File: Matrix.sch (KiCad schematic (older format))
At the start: 171 parts

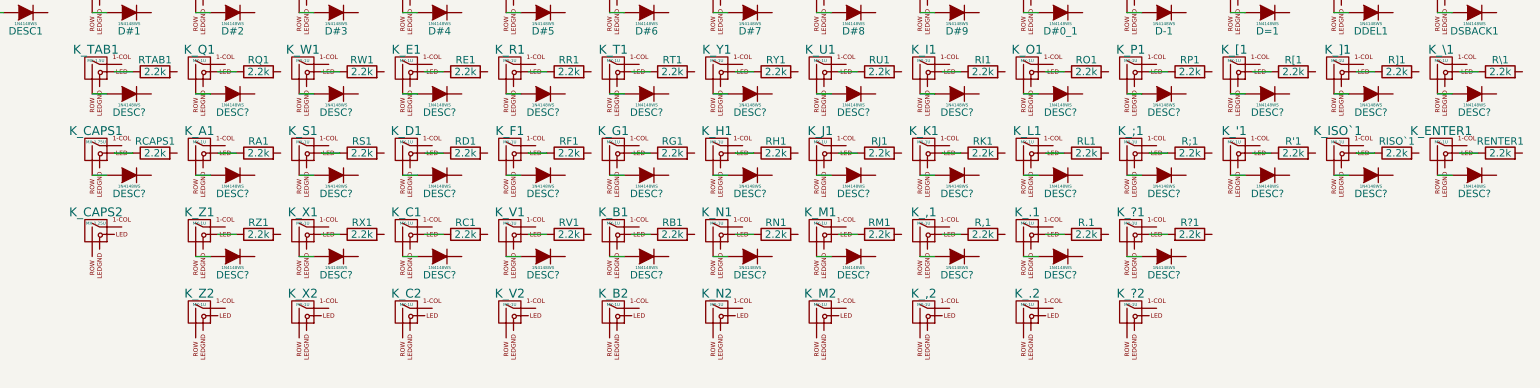
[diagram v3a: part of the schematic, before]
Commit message: Rename diodes
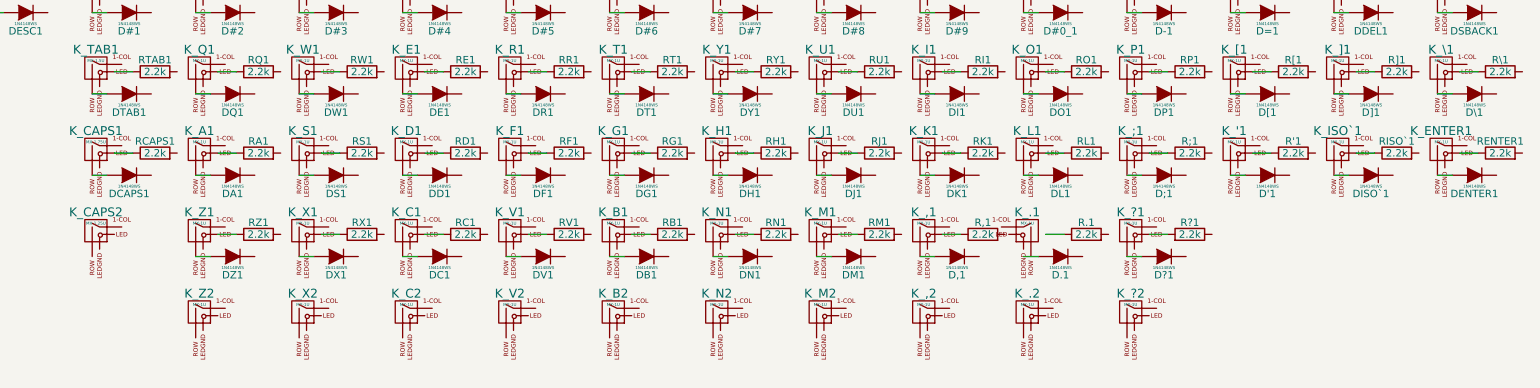
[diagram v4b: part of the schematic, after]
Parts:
- gave numbers to parts that had none: 38
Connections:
- net at K_.1.2 (ROW): no longer D.1.2 (A)
- net at K_.1.3 (LED): no longer R.1.1
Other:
- moved on the sheet: K_.1
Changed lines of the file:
@@
 $EndComp
 $Comp
-L D DESC?
+L D DTAB1
 U 1 1 597E3B71
 P 1725 2250
-F 0 "DESC?" H 1725 2375 50  0000 C CNN
+F 0 "DTAB1" H 1725 2375 50  0000 C CNN
 F 1 "1N4148WS" H 1725 2325 20  0000 C CNN
 F 2 "" H 1725 2250 50  0001 C CNN
@@
 $EndComp
 $Comp
-L D DESC?
+L D DQ1
 U 1 1 597E3B85
 P 2425 2250
-F 0 "DESC?" H 2425 2375 50  0000 C CNN
+F 0 "DQ1" H 2425 2375 50  0000 C CNN
 F 1 "1N4148WS" H 2425 2325 20  0000 C CNN
 F 2 "" H 2425 2250 50  0001 C CNN
@@
 $EndComp
 $Comp
-L D DESC?
+L D DW1
 U 1 1 597E3B99
 P 3125 2250
-F 0 "DESC?" H 3125 2375 50  0000 C CNN
+F 0 "DW1" H 3125 2375 50  0000 C CNN
 F 1 "1N4148WS" H 3125 2325 20  0000 C CNN
 F 2 "" H 3125 2250 50  0001 C CNN
@@
 $EndComp
 $Comp
-L D DESC?
+L D DE1
 U 1 1 597E3BAD
 P 3825 2250
-F 0 "DESC?" H 3825 2375 50  0000 C CNN
+F 0 "DE1" H 3825 2375 50  0000 C CNN
 F 1 "1N4148WS" H 3825 2325 20  0000 C CNN
 F 2 "" H 3825 2250 50  0001 C CNN
@@
 $EndComp
 $Comp
-L D DESC?
+L D DR1
 U 1 1 597E3BC1
 P 4525 2250
-F 0 "DESC?" H 4525 2375 50  0000 C CNN
+F 0 "DR1" H 4525 2375 50  0000 C CNN
 F 1 "1N4148WS" H 4525 2325 20  0000 C CNN
 F 2 "" H 4525 2250 50  0001 C CNN
@@
 $EndComp
 $Comp
-L D DESC?
+L D DT1
 U 1 1 597E3BD5
 P 5225 2250
-F 0 "DESC?" H 5225 2375 50  0000 C CNN
+F 0 "DT1" H 5225 2375 50  0000 C CNN
 F 1 "1N4148WS" H 5225 2325 20  0000 C CNN
 F 2 "" H 5225 2250 50  0001 C CNN
@@
 $EndComp
 $Comp
-L D DESC?
+L D DY1
 U 1 1 597E3BE9
 P 5925 2250
-F 0 "DESC?" H 5925 2375 50  0000 C CNN
+F 0 "DY1" H 5925 2375 50  0000 C CNN
 F 1 "1N4148WS" H 5925 2325 20  0000 C CNN
 F 2 "" H 5925 2250 50  0001 C CNN
@@
 $EndComp
 $Comp
-L D DESC?
+L D DU1
 U 1 1 597E3BFD
 P 6625 2250
-F 0 "DESC?" H 6625 2375 50  0000 C CNN
+F 0 "DU1" H 6625 2375 50  0000 C CNN
 F 1 "1N4148WS" H 6625 2325 20  0000 C CNN
 F 2 "" H 6625 2250 50  0001 C CNN
@@
 $EndComp
 $Comp
-L D DESC?
+L D DI1
 U 1 1 597E3C11
 P 7325 2250
-F 0 "DESC?" H 7325 2375 50  0000 C CNN
+F 0 "DI1" H 7325 2375 50  0000 C CNN
 F 1 "1N4148WS" H 7325 2325 20  0000 C CNN
 F 2 "" H 7325 2250 50  0001 C CNN
@@
 $EndComp
 $Comp
-L D DESC?
+L D DO1
 U 1 1 597E3C25
 P 8025 2250
-F 0 "DESC?" H 8025 2375 50  0000 C CNN
+F 0 "DO1" H 8025 2375 50  0000 C CNN
 F 1 "1N4148WS" H 8025 2325 20  0000 C CNN
 F 2 "" H 8025 2250 50  0001 C CNN
@@
 $EndComp
 $Comp
-L D DESC?
+L D DP1
 U 1 1 597E3C39
 P 8725 2250
-F 0 "DESC?" H 8725 2375 50  0000 C CNN
+F 0 "DP1" H 8725 2375 50  0000 C CNN
 F 1 "1N4148WS" H 8725 2325 20  0000 C CNN
 F 2 "" H 8725 2250 50  0001 C CNN
@@
 $EndComp
 $Comp
-L D DESC?
+L D D[1
 U 1 1 597E3C4D
 P 9425 2250
-F 0 "DESC?" H 9425 2375 50  0000 C CNN
+F 0 "D[1" H 9425 2375 50  0000 C CNN
 F 1 "1N4148WS" H 9425 2325 20  0000 C CNN
 F 2 "" H 9425 2250 50  0001 C CNN
@@
 $EndComp
 $Comp
-L D DESC?
+L D D]1
 U 1 1 597E3C61
 P 10125 2250
-F 0 "DESC?" H 10125 2375 50  0000 C CNN
+F 0 "D]1" H 10125 2375 50  0000 C CNN
 F 1 "1N4148WS" H 10125 2325 20  0000 C CNN
 F 2 "" H 10125 2250 50  0001 C CNN
@@
 $EndComp
 $Comp
-L D DESC?
+L D D\1
 U 1 1 597E3C75
 P 10825 2250
-F 0 "DESC?" H 10825 2375 50  0000 C CNN
+F 0 "D\\1" H 10825 2375 50  0000 C CNN
 F 1 "1N4148WS" H 10825 2325 20  0000 C CNN
 F 2 "" H 10825 2250 50  0001 C CNN
@@
 $EndComp
 $Comp
-L D DESC?
+L D DCAPS1
 U 1 1 597E5CB1
 P 1725 2800
-F 0 "DESC?" H 1725 2925 50  0000 C CNN
+F 0 "DCAPS1" H 1725 2925 50  0000 C CNN
 F 1 "1N4148WS" H 1725 2875 20  0000 C CNN
 F 2 "" H 1725 2800 50  0001 C CNN
@@
 $EndComp
 $Comp
-L D DESC?
+L D DA1
 U 1 1 597E5CC5
 P 2425 2800
-F 0 "DESC?" H 2425 2925 50  0000 C CNN
+F 0 "DA1" H 2425 2925 50  0000 C CNN
 F 1 "1N4148WS" H 2425 2875 20  0000 C CNN
 F 2 "" H 2425 2800 50  0001 C CNN
@@
 $EndComp
 $Comp
-L D DESC?
+L D DS1
 U 1 1 597E5CD9
 P 3125 2800
-F 0 "DESC?" H 3125 2925 50  0000 C CNN
+F 0 "DS1" H 3125 2925 50  0000 C CNN
 F 1 "1N4148WS" H 3125 2875 20  0000 C CNN
 F 2 "" H 3125 2800 50  0001 C CNN
@@
 $EndComp
 $Comp
-L D DESC?
+L D DD1
 U 1 1 597E5CED
 P 3825 2800
-F 0 "DESC?" H 3825 2925 50  0000 C CNN
+F 0 "DD1" H 3825 2925 50  0000 C CNN
 F 1 "1N4148WS" H 3825 2875 20  0000 C CNN
 F 2 "" H 3825 2800 50  0001 C CNN
@@
 $EndComp
 $Comp
-L D DESC?
+L D DF1
 U 1 1 597E5D01
 P 4525 2800
-F 0 "DESC?" H 4525 2925 50  0000 C CNN
+F 0 "DF1" H 4525 2925 50  0000 C CNN
 F 1 "1N4148WS" H 4525 2875 20  0000 C CNN
 F 2 "" H 4525 2800 50  0001 C CNN
@@
 $EndComp
 $Comp
-L D DESC?
+L D DG1
 U 1 1 597E5D15
 P 5225 2800
-F 0 "DESC?" H 5225 2925 50  0000 C CNN
+F 0 "DG1" H 5225 2925 50  0000 C CNN
 F 1 "1N4148WS" H 5225 2875 20  0000 C CNN
 F 2 "" H 5225 2800 50  0001 C CNN
@@
 $EndComp
 $Comp
-L D DESC?
+L D DH1
 U 1 1 597E5D29
 P 5925 2800
-F 0 "DESC?" H 5925 2925 50  0000 C CNN
+F 0 "DH1" H 5925 2925 50  0000 C CNN
 F 1 "1N4148WS" H 5925 2875 20  0000 C CNN
 F 2 "" H 5925 2800 50  0001 C CNN
@@
 $EndComp
 $Comp
-L D DESC?
+L D DJ1
 U 1 1 597E5D3D
 P 6625 2800
-F 0 "DESC?" H 6625 2925 50  0000 C CNN
+F 0 "DJ1" H 6625 2925 50  0000 C CNN
 F 1 "1N4148WS" H 6625 2875 20  0000 C CNN
 F 2 "" H 6625 2800 50  0001 C CNN
@@
 $EndComp
 $Comp
-L D DESC?
+L D DK1
 U 1 1 597E5D51
 P 7325 2800
-F 0 "DESC?" H 7325 2925 50  0000 C CNN
+F 0 "DK1" H 7325 2925 50  0000 C CNN
 F 1 "1N4148WS" H 7325 2875 20  0000 C CNN
 F 2 "" H 7325 2800 50  0001 C CNN
@@
 $EndComp
 $Comp
-L D DESC?
+L D DL1
 U 1 1 597E5D65
 P 8025 2800
-F 0 "DESC?" H 8025 2925 50  0000 C CNN
+F 0 "DL1" H 8025 2925 50  0000 C CNN
 F 1 "1N4148WS" H 8025 2875 20  0000 C CNN
 F 2 "" H 8025 2800 50  0001 C CNN
@@
 $EndComp
 $Comp
-L D DESC?
+L D D;1
 U 1 1 597E5D79
 P 8725 2800
-F 0 "DESC?" H 8725 2925 50  0000 C CNN
+F 0 "D;1" H 8725 2925 50  0000 C CNN
 F 1 "1N4148WS" H 8725 2875 20  0000 C CNN
 F 2 "" H 8725 2800 50  0001 C CNN
@@
 $EndComp
 $Comp
-L D DESC?
+L D D'1
 U 1 1 597E5D8D
 P 9425 2800
-F 0 "DESC?" H 9425 2925 50  0000 C CNN
+F 0 "D'1" H 9425 2925 50  0000 C CNN
 F 1 "1N4148WS" H 9425 2875 20  0000 C CNN
 F 2 "" H 9425 2800 50  0001 C CNN
@@
 $EndComp
 $Comp
-L D DESC?
+L D DISO`1
 U 1 1 597E5DA1
 P 10125 2800
-F 0 "DESC?" H 10125 2925 50  0000 C CNN
+F 0 "DISO`1" H 10125 2925 50  0000 C CNN
 F 1 "1N4148WS" H 10125 2875 20  0000 C CNN
 F 2 "" H 10125 2800 50  0001 C CNN
@@
 $EndComp
 $Comp
-L D DESC?
+L D DENTER1
 U 1 1 597E5DB5
 P 10825 2800
-F 0 "DESC?" H 10825 2925 50  0000 C CNN
+F 0 "DENTER1" H 10825 2925 50  0000 C CNN
 F 1 "1N4148WS" H 10825 2875 20  0000 C CNN
 F 2 "" H 10825 2800 50  0001 C CNN
@@
 $EndComp
 $Comp
-L D DESC?
+L D DZ1
 U 1 1 597E5DDD
 P 2425 3350
-F 0 "DESC?" H 2425 3475 50  0000 C CNN
+F 0 "DZ1" H 2425 3475 50  0000 C CNN
 F 1 "1N4148WS" H 2425 3425 20  0000 C CNN
 F 2 "" H 2425 3350 50  0001 C CNN
@@
 $EndComp
 $Comp
-L D DESC?
+L D DX1
 U 1 1 597E5DF1
 P 3125 3350
-F 0 "DESC?" H 3125 3475 50  0000 C CNN
+F 0 "DX1" H 3125 3475 50  0000 C CNN
 F 1 "1N4148WS" H 3125 3425 20  0000 C CNN
 F 2 "" H 3125 3350 50  0001 C CNN
@@
 $EndComp
 $Comp
-L D DESC?
+L D DC1
 U 1 1 597E5E05
 P 3825 3350
-F 0 "DESC?" H 3825 3475 50  0000 C CNN
+F 0 "DC1" H 3825 3475 50  0000 C CNN
 F 1 "1N4148WS" H 3825 3425 20  0000 C CNN
 F 2 "" H 3825 3350 50  0001 C CNN
@@
 $EndComp
 $Comp
-L D DESC?
+L D DV1
 U 1 1 597E5E19
 P 4525 3350
-F 0 "DESC?" H 4525 3475 50  0000 C CNN
+F 0 "DV1" H 4525 3475 50  0000 C CNN
 F 1 "1N4148WS" H 4525 3425 20  0000 C CNN
 F 2 "" H 4525 3350 50  0001 C CNN
@@
 $EndComp
 $Comp
-L D DESC?
+L D DB1
 U 1 1 597E5E2D
 P 5225 3350
-F 0 "DESC?" H 5225 3475 50  0000 C CNN
+F 0 "DB1" H 5225 3475 50  0000 C CNN
 F 1 "1N4148WS" H 5225 3425 20  0000 C CNN
 F 2 "" H 5225 3350 50  0001 C CNN
@@
 $EndComp
 $Comp
-L D DESC?
+L D DN1
 U 1 1 597E5E41
 P 5925 3350
-F 0 "DESC?" H 5925 3475 50  0000 C CNN
+F 0 "DN1" H 5925 3475 50  0000 C CNN
 F 1 "1N4148WS" H 5925 3425 20  0000 C CNN
 F 2 "" H 5925 3350 50  0001 C CNN
@@
 $EndComp
 $Comp
-L D DESC?
+L D DM1
 U 1 1 597E5E55
 P 6625 3350
-F 0 "DESC?" H 6625 3475 50  0000 C CNN
+F 0 "DM1" H 6625 3475 50  0000 C CNN
 F 1 "1N4148WS" H 6625 3425 20  0000 C CNN
 F 2 "" H 6625 3350 50  0001 C CNN
@@
 $EndComp
 $Comp
-L D DESC?
+L D D,1
 U 1 1 597E5E69
 P 7325 3350
-F 0 "DESC?" H 7325 3475 50  0000 C CNN
+F 0 "D,1" H 7325 3475 50  0000 C CNN
 F 1 "1N4148WS" H 7325 3425 20  0000 C CNN
 F 2 "" H 7325 3350 50  0001 C CNN
@@
 F 3 "" H 7775 3150 60  0001 C CNN
 	1    7800 3175
-	1    0    0    -1
+	-1   0    0    -1
 $EndComp
 $Comp
@@
 $EndComp
 $Comp
-L D DESC?
+L D D.1
 U 1 1 597E5E7D
 P 8025 3350
-F 0 "DESC?" H 8025 3475 50  0000 C CNN
+F 0 "D.1" H 8025 3475 50  0000 C CNN
 F 1 "1N4148WS" H 8025 3425 20  0000 C CNN
 F 2 "" H 8025 3350 50  0001 C CNN
@@
 $EndComp
 $Comp
-L D DESC?
+L D D?1
 U 1 1 597E5E91
 P 8725 3350
-F 0 "DESC?" H 8725 3475 50  0000 C CNN
+F 0 "D?1" H 8725 3475 50  0000 C CNN
 F 1 "1N4148WS" H 8725 3425 20  0000 C CNN
 F 2 "" H 8725 3350 50  0001 C CNN

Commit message: Wire cols
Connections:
- net COL0: now also K_ESC1.1 (COL)
- net COL1: now also K_#1.1 (COL), K_#2.1 (COL), K_A1.1 (COL), K_CAPS1.1 (COL), K_CAPS2.1 (COL), K_Q1.1 (COL), K_TAB1.1 (COL), K_Z1.1 (COL), K_Z2.1 (COL)
- net COL2: now also K_#3.1 (COL), K_#4.1 (COL), K_C1.1 (COL), K_C2.1 (COL), K_D1.1 (COL), K_E1.1 (COL), K_S1.1 (COL), K_W1.1 (COL), K_X1.1 (COL), K_X2.1 (COL)
- net COL3: now also K_#5.1 (COL), K_#6.1 (COL), K_B1.1 (COL), K_B2.1 (COL), K_F1.1 (COL), K_G1.1 (COL), K_R1.1 (COL), K_T1.1 (COL), K_V1.1 (COL), K_V2.1 (COL)
- net COL4: now also K_#7.1 (COL), K_#8.1 (COL), K_H1.1 (COL), K_J1.1 (COL), K_M1.1 (COL), K_M2.1 (COL), K_N1.1 (COL), K_N2.1 (COL), K_U1.1 (COL), K_Y1.1 (COL)
- net COL5: now also K_#0_1.1 (COL), K_#9.1 (COL), K_,1.1 (COL), K_,2.1 (COL), K_.1.1 (COL), K_.2.1 (COL), K_I1.1 (COL), K_K1.1 (COL), K_L1.1 (COL), K_O1.1 (COL)
- net COL6: now also K_'1.1 (COL), K_-1.1 (COL), K_;1.1 (COL), K_=1.1 (COL), K_?1.1 (COL), K_?2.1 (COL), K_P1.1 (COL), K_[1.1 (COL)
- net COL7: now also K_DEL1.1 (COL), K_ENTER1.1 (COL), K_ISO`1.1 (COL), K_SBACK1.1 (COL), K_\1.1 (COL), K_]1.1 (COL)
- net at K_.1.2 (ROW): now also D.1.2 (A)
- net at K_.1.3 (LED): now also R.1.1
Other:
- moved on the sheet: K_.1

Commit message: Increase sheet size
Components were falling off the edge
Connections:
- net at K_#2.4 (LEDGND): now also K_#0_1.4 (LEDGND), K_#1.4 (LEDGND), K_#3.4 (LEDGND), K_#4.4 (LEDGND), K_#5.4 (LEDGND), K_#6.4 (LEDGND), K_#7.4 (LEDGND), K_#8.4 (LEDGND), K_#9.4 (LEDGND), K_-1.4 (LEDGND), K_=1.4 (LEDGND), K_DEL1.4 (LEDGND), K_SBACK1.4 (LEDGND)
- net at K_TAB1.4 (LEDGND): now also K_E1.4 (LEDGND), K_I1.4 (LEDGND), K_O1.4 (LEDGND), K_P1.4 (LEDGND), K_Q1.4 (LEDGND), K_R1.4 (LEDGND), K_T1.4 (LEDGND), K_U1.4 (LEDGND), K_W1.4 (LEDGND), K_Y1.4 (LEDGND), K_[1.4 (LEDGND), K_\1.4 (LEDGND), K_]1.4 (LEDGND)
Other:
- moved on the sheet: D#0_1, D#1, D#2, D#3, D#4, D#5, D#6, D#7, D#8, D#9, D'1, D,1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

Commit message: Wire LEDGND
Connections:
- net LEDGND: now also K_#0_1.4 (LEDGND), K_#1.4 (LEDGND), K_#2.4 (LEDGND), K_#3.4 (LEDGND), K_#4.4 (LEDGND), K_#5.4 (LEDGND), K_#6.4 (LEDGND), K_#7.4 (LEDGND), K_#8.4 (LEDGND), K_#9.4 (LEDGND), K_'1.4 (LEDGND), K_,1.4 (LEDGND), K_,2.4 (LEDGND), K_-1.4 (LEDGND), K_.1.4 (LEDGND), K_.2.4 (LEDGND), K_;1.4 (LEDGND), K_=1.4 (LEDGND), K_?1.4 (LEDGND), K_?2.4 (LEDGND), K_A1.4 (LEDGND), K_B1.4 (LEDGND), K_B2.4 (LEDGND), K_C1.4 (LEDGND), K_C2.4 (LEDGND), K_CAPS1.4 (LEDGND), K_CAPS2.4 (LEDGND), K_D1.4 (LEDGND), K_DEL1.4 (LEDGND), K_E1.4 (LEDGND), K_ENTER1.4 (LEDGND), K_ESC1.4 (LEDGND), K_F1.4 (LEDGND), K_G1.4 (LEDGND), K_H1.4 (LEDGND), K_I1.4 (LEDGND), K_ISO`1.4 (LEDGND), K_J1.4 (LEDGND), K_K1.4 (LEDGND), K_L1.4 (LEDGND), K_M1.4 (LEDGND), K_M2.4 (LEDGND), K_N1.4 (LEDGND), K_N2.4 (LEDGND), K_O1.4 (LEDGND), K_P1.4 (LEDGND), K_Q1.4 (LEDGND), K_R1.4 (LEDGND), K_S1.4 (LEDGND), K_SBACK1.4 (LEDGND), K_T1.4 (LEDGND), K_TAB1.4 (LEDGND), K_U1.4 (LEDGND), K_V1.4 (LEDGND), K_V2.4 (LEDGND), K_W1.4 (LEDGND), K_X1.4 (LEDGND), K_X2.4 (LEDGND), K_Y1.4 (LEDGND), K_Z1.4 (LEDGND), K_Z2.4 (LEDGND), K_[1.4 (LEDGND), K_\1.4 (LEDGND), K_]1.4 (LEDGND)
- net at DCAPS1.2 (A), K_CAPS1.2 (ROW): now also K_CAPS2.2 (ROW)
- net at K_CAPS1.3 (LED), RCAPS1.1: now also K_CAPS2.3 (LED)
- net at DZ1.2 (A), K_Z1.2 (ROW): now also K_Z2.2 (ROW)
- net at K_Z1.3 (LED), RZ1.1: now also K_Z2.3 (LED)
- net at DX1.2 (A), K_X1.2 (ROW): now also K_X2.2 (ROW)
- net at K_X1.3 (LED), RX1.1: now also K_X2.3 (LED)
- net at DC1.2 (A), K_C1.2 (ROW): now also K_C2.2 (ROW)
- net at K_C1.3 (LED), RC1.1: now also K_C2.3 (LED)
- net at DV1.2 (A), K_V1.2 (ROW): now also K_V2.2 (ROW)
- net at K_V1.3 (LED), RV1.1: now also K_V2.3 (LED)
- net at DB1.2 (A), K_B1.2 (ROW): now also K_B2.2 (ROW)
- net at K_B1.3 (LED), RB1.1: now also K_B2.3 (LED)
- net at DN1.2 (A), K_N1.2 (ROW): now also K_N2.2 (ROW)
- net at K_N1.3 (LED), RN1.1: now also K_N2.3 (LED)
- net at DM1.2 (A), K_M1.2 (ROW): now also K_M2.2 (ROW)
- net at K_M1.3 (LED), RM1.1: now also K_M2.3 (LED)
- net at D,1.2 (A), K_,1.2 (ROW): now also K_,2.2 (ROW)
- net at K_,1.3 (LED), R,1.1: now also K_,2.3 (LED)
- net at D.1.2 (A), K_.1.2 (ROW): now also K_.2.2 (ROW)
- net at K_.1.3 (LED), R.1.1: now also K_.2.3 (LED)
- net at D?1.2 (A), K_?1.2 (ROW): now also K_?2.2 (ROW)
- net at K_?1.3 (LED), R?1.2: now also K_?2.3 (LED)
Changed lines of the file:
@@
 F7 "leftmodsrow2" I R 5675 6525 60
 $EndSheet
-Text GLabel 1075 2525 0    60   Input ~ 0
+Text GLabel 2350 2800 0    60   Input ~ 0
 LEDGND
 $Comp
@@
 	13125 2800 13125 2700
 Wire Wire Line
-	4025 2800 13125 2800
+	2350 2800 13125 2800
 Wire Wire Line
 	12425 2800 12425 2700
@@
 	13125 3350 13125 3250
 Wire Wire Line
-	4025 3350 13125 3350
+	2350 3350 13125 3350
 Wire Wire Line
 	12425 3350 12425 3250
@@
 	4025 3350 4025 3250
 Connection ~ 4725 3350
+Wire Wire Line
+	13125 3900 13125 3800
+Wire Wire Line
+	2350 3900 13125 3900
+Wire Wire Line
+	12425 3900 12425 3800
+Wire Wire Line
+	11725 3900 11725 3800
+Connection ~ 12425 3900
+Wire Wire Line
+	11025 3900 11025 3800
+Connection ~ 11725 3900
+Wire Wire Line
+	10325 3900 10325 3800
+Connection ~ 11025 3900
+Wire Wire Line
+	9625 3900 9625 3800
+Connection ~ 10325 3900
+Wire Wire Line
+	8925 3900 8925 3800
+Connection ~ 9625 3900
+Wire Wire Line
+	8225 3900 8225 3800
+Connection ~ 8925 3900
+Wire Wire Line
+	7525 3900 7525 3800
+Connection ~ 8225 3900
+Wire Wire Line
+	6825 3900 6825 3800
+Connection ~ 7525 3900
+Wire Wire Line
+	6125 3900 6125 3800
+Connection ~ 6825 3900
+Wire Wire Line
+	5425 3900 5425 3800
+Connection ~ 6125 3900
+Wire Wire Line
+	4725 3900 4725 3800
+Connection ~ 5425 3900
+Wire Wire Line
+	4025 3800 4025 4350
+Connection ~ 4725 3900
+Wire Wire Line
+	11025 4350 11025 4900
+Wire Wire Line
+	2350 4450 11025 4450
+Wire Wire Line
+	10325 4350 10325 4900
+Wire Wire Line
+	9625 4350 9625 4900
+Connection ~ 10325 4450
+Wire Wire Line
+	8925 4350 8925 4900
+Connection ~ 9625 4450
+Wire Wire Line
+	8225 4350 8225 4900
+Connection ~ 8925 4450
+Wire Wire Line
+	7525 4350 7525 4900
+Connection ~ 8225 4450
+Wire Wire Line
+	6825 4350 6825 4900
+Connection ~ 7525 4450
+Wire Wire Line
+	6125 4350 6125 4900
+Connection ~ 6825 4450
+Wire Wire Line
+	5425 4350 5425 4900
+Connection ~ 6125 4450
+Wire Wire Line
+	4725 4350 4725 4900
+Connection ~ 5425 4450
+Wire Wire Line
+	3975 4400 3975 3850
+Connection ~ 4025 3900
+Wire Wire Line
+	4125 3700 4125 4250
+Wire Wire Line
+	4675 4400 4675 4950
+Connection ~ 4725 4450
+Wire Wire Line
+	4825 4250 4825 4800
+Wire Wire Line
+	5375 4400 5375 4950
+Wire Wire Line
+	5525 4250 5525 4800
+Wire Wire Line
+	6075 4950 6075 4400
+Wire Wire Line
+	6225 4250 6225 4800
+Wire Wire Line
+	6775 4950 6775 4400
+Wire Wire Line
+	6925 4250 6925 4800
+Wire Wire Line
+	7475 4950 7475 4400
+Wire Wire Line
+	7625 4250 7625 4800
+Wire Wire Line
+	8175 4950 8175 4400
+Wire Wire Line
+	8325 4250 8325 4800
+Wire Wire Line
+	9025 4250 9025 4800
+Wire Wire Line
+	8875 4950 8875 4400
+Wire Wire Line
+	9575 4950 9575 4400
+Wire Wire Line
+	9725 4250 9725 4800
+Wire Wire Line
+	10275 4950 10275 4400
+Wire Wire Line
+	10425 4250 10425 4800
+Wire Wire Line
+	10975 4950 10975 4400
+Connection ~ 11025 4450
+Wire Wire Line
+	11125 4250 11125 4800
+Wire Wire Line
+	3325 2800 3325 2700
+Connection ~ 4025 2800
+Wire Wire Line
+	2350 2800 2350 4450
+Connection ~ 4025 3350
+Connection ~ 3325 2800
+Connection ~ 2350 3350
+Connection ~ 2350 3900
 $EndSCHEMATC
